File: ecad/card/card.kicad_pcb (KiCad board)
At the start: 4 copper layers, 133.4 x 32.2 mm, 135 parts, among them J1 Conn_01x03_Pin, J2 USB4105-GF-A, J3 10145226-0241N13LF, J4 Conn_01x03_Pin, SW1 SW_Push, SW2 SW_Push, U1 W25Q128JVS, U2 RP2350_80QFN, U3 MCP23017_SO, U4 NCP1117-3.3_SOT223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

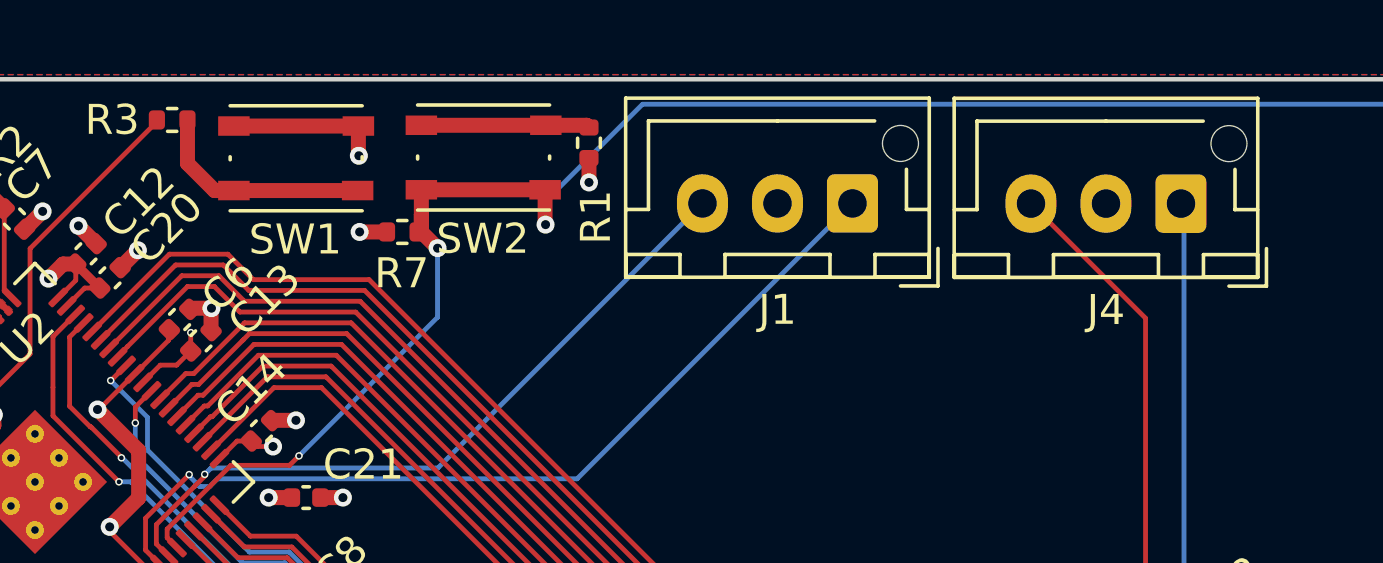
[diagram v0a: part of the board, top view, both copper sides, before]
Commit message: add labels on card
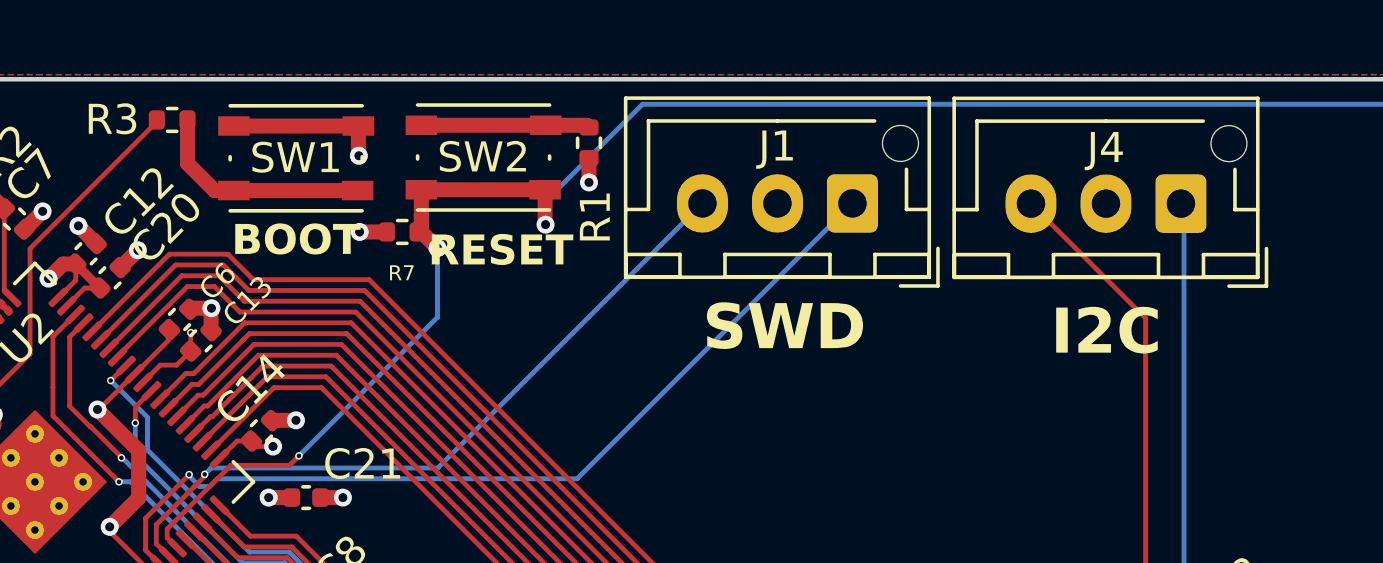
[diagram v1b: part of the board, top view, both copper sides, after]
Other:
- board text added: "BOOT"
- board text added: "I2C"
- board text added: "RESET"
- board text added: "SWD"

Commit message: card connector, diode changes
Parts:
- added J5: Conn_01x03_Pin, Connector_JST:JST_XH_S3B-XH-A-1_1x03_P2.50mm_Horizontal, F.Cu at (177.7, 57.4)
- D1: footprint Diode_SMD:D_0402_1005Metric -> Library:DO-214BA_MCH-M
- J1, J4: footprint Connector_JST:JST_XH_B3B-XH-AM_1x03_P2.50mm_Vertical -> Connector_JST:JST_XH_S3B-XH-A-1_1x03_P2.50mm_Horizontal
- moved R9 5.99 mm to (53.5, 54.1)
- moved R10 5.26 mm to (65.1, 55.4)
- moved D1 5.20 mm to (57.2, 60.1), turned to 0 degrees
- moved C22 5.03 mm to (53.8, 63.5), turned to -90 degrees
- moved J1 4.12 mm to (103.2, 57.4)
- moved J4 4.12 mm to (114.2, 57.4)
- moved C23 2.43 mm to (58.5, 73.2)
- moved U4 2.43 mm to (57.9, 68.0)
- moved C3 0.45 mm to (61.6, 60.8), turned to -90 degrees
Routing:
- net /I2C1_SDA: track 32.9 -> 70.3 mm, vias 2 -> 3
- net /I2C1_SCL: track 34.3 -> 66.2 mm, vias 2 -> 3
- net Net-(J2-CC2): track 1.37 -> 6.25 mm
- net Net-(J2-CC1): track 1.37 -> 5.91 mm
- net /I2C0_SDA: track 28.6 -> 24.7 mm
- net /I2C0_SCL: track 29.7 -> 25.8 mm
- net VBUS: track 2.56 -> 5.11 mm
- net Net-(J1-Pin_3): track 23.9 -> 21.8 mm
- net Net-(J1-Pin_1): track 30.0 -> 28.0 mm
- net 3.3V: track 214.0 -> 215.7 mm, vias 35 -> 39
- net /USB_D+: track 15.2 -> 13.9 mm
- net GND: track 211.5 -> 212.7 mm, vias 51 -> 52
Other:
- board text added: "I2C 0 UART 0"
- board text added: "I2C 1 UART 1"
- board text removed: "I2C"

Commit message: card silkscreen
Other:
- board text added: "Brian Lu Nathan Huang Seth Deegan Caleb Shinkle"
- board text added: "αCassiopeiae Card Team 15"
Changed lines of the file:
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@@
 	(footprint "Button_Switch_SMD:SW_Push_1P1T_NO_Vertical_Wuerth_434133025816"
 		(layer "F.Cu")
-		(at 85.005871 51.789126)
+		(at 85.005871 51.775)
 		(descr "https://katalog.we-online.com/em/datasheet/434133025816.pdf")
 		(tags "tactile switch Wurth Wuerth")
@@
 	(footprint "Button_Switch_SMD:SW_Push_1P1T_NO_Vertical_Wuerth_434133025816"
 		(layer "F.Cu")
-		(at 91.254271 51.763726)
+		(at 91.254271 51.775)
 		(descr "https://katalog.we-online.com/em/datasheet/434133025816.pdf")
 		(tags "tactile switch Wurth Wuerth")
@@
 		)
 	)
+	(gr_text "Brian Lu Nathan Huang Seth Deegan Caleb Shinkle"
+		(at 179.849944 66.25817 0)
+		(layer "B.SilkS")
+		(effects
+			(font
+				(size 2 2)
+				(thickness 0.3)
+				(bold yes)
+			)
+			(justify left bottom mirror)
+		)
+	)
 	(gr_text "I2C 0\nUART 0"
-		(at 111.650129 61.805674 0)
-		(layer "F.SilkS")
+		(at 111.650129 50.005674 0)
+		(layer "B.SilkS" knockout)
 		(effects
 			(font
@@
 				(bold yes)
 			)
-			(justify bottom)
+			(justify top mirror)
+		)
+	)
+	(gr_text "I2C 0\nUART 0"
+		(at 59.5 50 0)
+		(layer "B.SilkS" knockout)
+		(effects
+			(font
+				(size 1 1)
+				(thickness 0.25)
+				(bold yes)
+			)
+			(justify top mirror)
 		)
 	)
 	(gr_text "I2C 1\nUART 1"
-		(at 175.2 61.8 0)
-		(layer "F.SilkS")
+		(at 175.2 50 0)
+		(layer "B.SilkS" knockout)
 		(effects
 			(font
@@
 				(bold yes)
 			)
-			(justify bottom)
+			(justify top mirror)
+		)
+	)
+	(gr_text "αCassiopeiae Card\nTeam 15"
+		(at 179.6 76.2 0)
+		(layer "B.SilkS")
+		(effects
+			(font
+				(size 3 3)
+				(thickness 0.6)
+				(bold yes)
+			)
+			(justify left bottom mirror)
 		)
 	)
 	(gr_text "SWD"
-		(at 100.7 61.8 0)
-		(layer "F.SilkS")
+		(at 100.7 50 0)
+		(layer "B.SilkS" knockout)
 		(effects
 			(font
@@
 				(bold yes)
 			)
-			(justify bottom)
+			(justify top mirror)
 		)
 	)
 	(gr_text "RESET"
-		(at 90 55.1 0)
-		(layer "F.SilkS")
+		(at 91.254271 50.025 0)
+		(layer "B.SilkS" knockout)
 		(effects
 			(font
@@
 				(bold yes)
 			)
-			(justify left bottom)
+			(justify top mirror)
 		)
 	)
 	(gr_text "BOOT"
-		(at 82.85 55.1 0)
-		(layer "F.SilkS")
+		(at 85.005871 50.025 0)
+		(layer "B.SilkS" knockout)
 		(effects
 			(font
@@
 				(bold yes)
 			)
-			(justify left bottom)
+			(justify top mirror)
 		)
 	)
@@
 		(min_thickness 0.15)
 		(filled_areas_thickness no)
-		(fill yes
+		(fill
 			(thermal_gap 0.5)
 			(thermal_bridge_width 0.5)
@@
 		(min_thickness 0.1)
 		(filled_areas_thickness no)
-		(fill yes
+		(fill
 			(thermal_gap 0.5)
 			(thermal_bridge_width 0.5)
@@
 		(min_thickness 0.1)
 		(filled_areas_thickness no)
-		(fill yes
+		(fill
 			(thermal_gap 0.5)
 			(thermal_bridge_width 0.5)
@@
 		(min_thickness 0.1)
 		(filled_areas_thickness no)
-		(fill yes
+		(fill
 			(thermal_gap 0.5)
 			(thermal_bridge_width 0.5)
@@
 		(min_thickness 0.25)
 		(filled_areas_thickness no)
-		(fill yes
+		(fill
 			(thermal_gap 0.5)
 			(thermal_bridge_width 0.5)
@@
 		(min_thickness 0.25)
 		(filled_areas_thickness no)
-		(fill yes
+		(fill
 			(thermal_gap 0.5)
 			(thermal_bridge_width 0.5)
@@
 		(min_thickness 0.1)
 		(filled_areas_thickness no)
-		(fill yes
+		(fill
 			(thermal_gap 0.5)
 			(thermal_bridge_width 0.5)
@@
 		(min_thickness 0.15)
 		(filled_areas_thickness no)
-		(fill yes
+		(fill
 			(thermal_gap 0.5)
 			(thermal_bridge_width 0.5)
@@
 		(min_thickness 0.15)
 		(filled_areas_thickness no)
-		(fill yes
+		(fill
 			(thermal_gap 0.5)
 			(thermal_bridge_width 0.5)
@@
 		(min_thickness 0.1)
 		(filled_areas_thickness no)
-		(fill yes
+		(fill
 			(thermal_gap 0.5)
 			(thermal_bridge_width 0.5)
@@
 		(min_thickness 0.15)
 		(filled_areas_thickness no)
-		(fill yes
+		(fill
 			(thermal_gap 0.5)
 			(thermal_bridge_width 0.5)
@@
 		(min_thickness 0.15)
 		(filled_areas_thickness no)
-		(fill yes
+		(fill
 			(thermal_gap 0.5)
 			(thermal_bridge_width 0.5)
@@
 		(min_thickness 0.15)
 		(filled_areas_thickness no)
-		(fill yes
+		(fill
 			(thermal_gap 0.5)
 			(thermal_bridge_width 0.5)
@@
 		(min_thickness 0.15)
 		(filled_areas_thickness no)
-		(fill yes
+		(fill
 			(thermal_gap 0.5)
 			(thermal_bridge_width 0.5)

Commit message: general team number silkscreen
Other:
- board text added: "rev. 01 3/14/2025"
- board text added: "αCassiopeiae 8800 Computer Card Board ECE 477 Team 15"
- board text removed: "αCassiopeiae Card Team 15"
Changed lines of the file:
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@@
 				(material "Direct Printing")
 			)
-			(copper_finish "HAL lead-free")
+			(copper_finish "ENIG")
 			(dielectric_constraints no)
 			(edge_connector yes)
@@
 		)
 		(property "Footprint" "Library:DO-214BA_MCH-M"
-			(at 0 0 360)
+			(at 0 0 0)
 			(layer "F.Fab")
 			(hide yes)
@@
 		)
 		(property "Datasheet" ""
-			(at 0 0 360)
+			(at 0 0 0)
 			(layer "F.Fab")
 			(hide yes)
@@
 		)
 		(property "Description" "Schottky diode"
-			(at 0 0 360)
+			(at 0 0 0)
 			(layer "F.Fab")
 			(hide yes)
@@
 		(tags "connector JST XH horizontal")
 		(property "Reference" "J5"
-			(at 2.5 -5.1 360)
+			(at 2.5 -5.1 0)
 			(layer "F.SilkS")
 			(effects
@@
 		)
 		(property "Value" "Conn_01x03_Pin"
-			(at 2.5 8.8 360)
+			(at 2.5 8.8 0)
 			(layer "F.Fab")
 			(effects
@@
 		)
 		(fp_text user "${REFERENCE}"
-			(at 2.5 1.85 360)
+			(at 2.5 1.85 0)
 			(layer "F.Fab")
 			(effects
@@
 		(tags "capacitor")
 		(property "Reference" "C3"
-			(at 0.4652 -1.4806 360)
+			(at 0.4652 -1.4806 0)
 			(layer "F.SilkS")
 			(hide yes)
@@
 	)
 	(gr_text "Brian Lu Nathan Huang Seth Deegan Caleb Shinkle"
-		(at 179.849944 66.25817 0)
+		(at 180.2 66.25817 0)
 		(layer "B.SilkS")
 		(effects
@@
 		)
 	)
+	(gr_text "rev. 01 3/14/2025"
+		(at 53.5 76.2 0)
+		(layer "B.SilkS")
+		(effects
+			(font
+				(size 2 2)
+				(thickness 0.3)
+				(bold yes)
+			)
+			(justify right bottom mirror)
+		)
+	)
 	(gr_text "I2C 1\nUART 1"
 		(at 175.2 50 0)
@@
 		)
 	)
-	(gr_text "αCassiopeiae Card\nTeam 15"
-		(at 179.6 76.2 0)
+	(gr_text "αCassiopeiae 8800 Computer Card Board\nECE 477 Team 15"
+		(at 180.4 76.2 0)
 		(layer "B.SilkS")
 		(effects
@@
 		(min_thickness 0.15)
 		(filled_areas_thickness no)
-		(fill
+		(fill yes
 			(thermal_gap 0.5)
 			(thermal_bridge_width 0.5)
@@
 		(min_thickness 0.1)
 		(filled_areas_thickness no)
-		(fill
+		(fill yes
 			(thermal_gap 0.5)
 			(thermal_bridge_width 0.5)
@@
 		(min_thickness 0.1)
 		(filled_areas_thickness no)
-		(fill
+		(fill yes
 			(thermal_gap 0.5)
 			(thermal_bridge_width 0.5)
@@
 		(min_thickness 0.1)
 		(filled_areas_thickness no)
-		(fill
+		(fill yes
 			(thermal_gap 0.5)
 			(thermal_bridge_width 0.5)
@@
 		(min_thickness 0.25)
 		(filled_areas_thickness no)
-		(fill
+		(fill yes
 			(thermal_gap 0.5)
 			(thermal_bridge_width 0.5)
@@
 		(min_thickness 0.25)
 		(filled_areas_thickness no)
-		(fill
+		(fill yes
 			(thermal_gap 0.5)
 			(thermal_bridge_width 0.5)
@@
 		(min_thickness 0.1)
 		(filled_areas_thickness no)
-		(fill
+		(fill yes
 			(thermal_gap 0.5)
 			(thermal_bridge_width 0.5)
@@
 		(min_thickness 0.15)
 		(filled_areas_thickness no)
-		(fill
+		(fill yes
 			(thermal_gap 0.5)
 			(thermal_bridge_width 0.5)
@@
 		(min_thickness 0.15)
 		(filled_areas_thickness no)
-		(fill
+		(fill yes
 			(thermal_gap 0.5)
 			(thermal_bridge_width 0.5)
@@
 		(min_thickness 0.1)
 		(filled_areas_thickness no)
-		(fill
+		(fill yes
 			(thermal_gap 0.5)
 			(thermal_bridge_width 0.5)
@@
 		(min_thickness 0.15)
 		(filled_areas_thickness no)
-		(fill
+		(fill yes
 			(thermal_gap 0.5)
 			(thermal_bridge_width 0.5)
@@
 		(min_thickness 0.15)
 		(filled_areas_thickness no)
-		(fill
+		(fill yes
 			(thermal_gap 0.5)
 			(thermal_bridge_width 0.5)
@@
 		(min_thickness 0.15)
 		(filled_areas_thickness no)
-		(fill
+		(fill yes
 			(thermal_gap 0.5)
 			(thermal_bridge_width 0.5)
@@
 		(min_thickness 0.15)
 		(filled_areas_thickness no)
-		(fill
+		(fill yes
 			(thermal_gap 0.5)
 			(thermal_bridge_width 0.5)
